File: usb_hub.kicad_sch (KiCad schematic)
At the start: 6 parts, among them U501 FE1.1s, Y501 12MHz

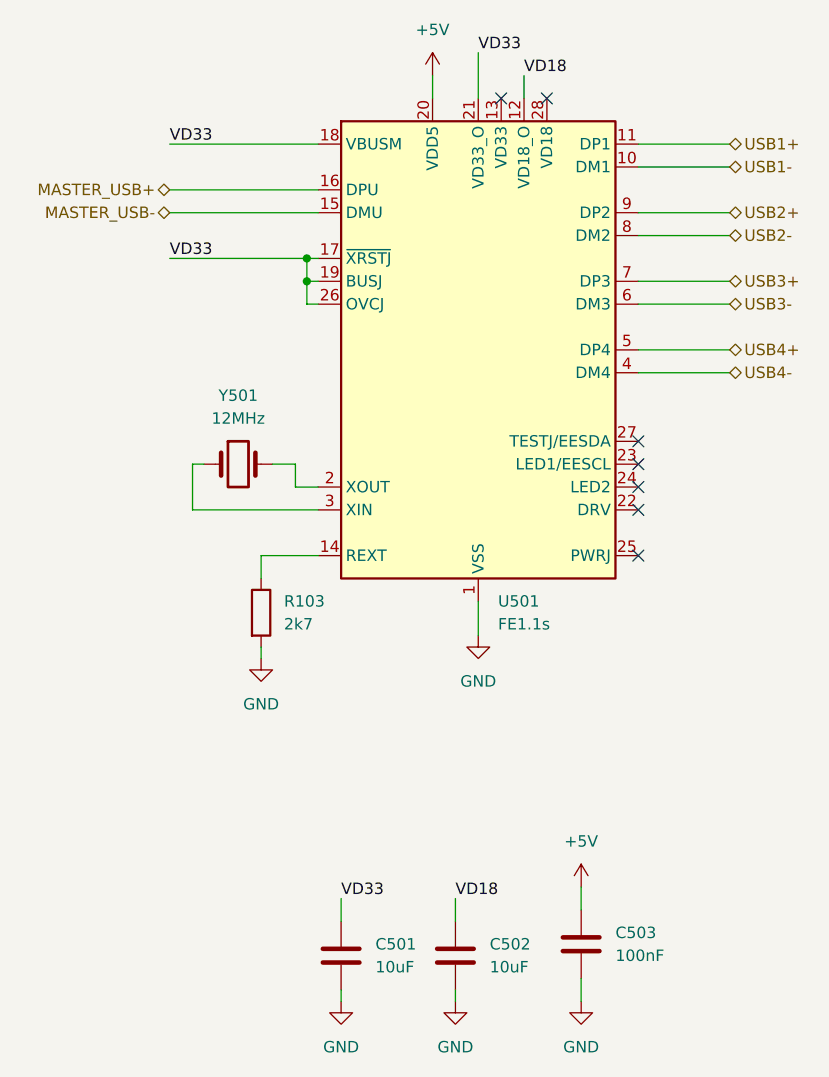
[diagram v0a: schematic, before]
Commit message: Update USB-C and USB-Hub Schematics with New Titles and Reference Changes
- Changed title from "DebugBoard" to "USB-C" in usb_c.kicad_sch.
- Changed title from "DebugBoard" to "USB-Hub" in usb_hub.kicad_sch.
- Updated multiple component references in usb_c.kicad_sch to new identifiers (#PWR0301 to #PWR0312, D301, U301, etc.).
- Updated component reference from "R103" to "R501" in usb_hub.kicad_sch.
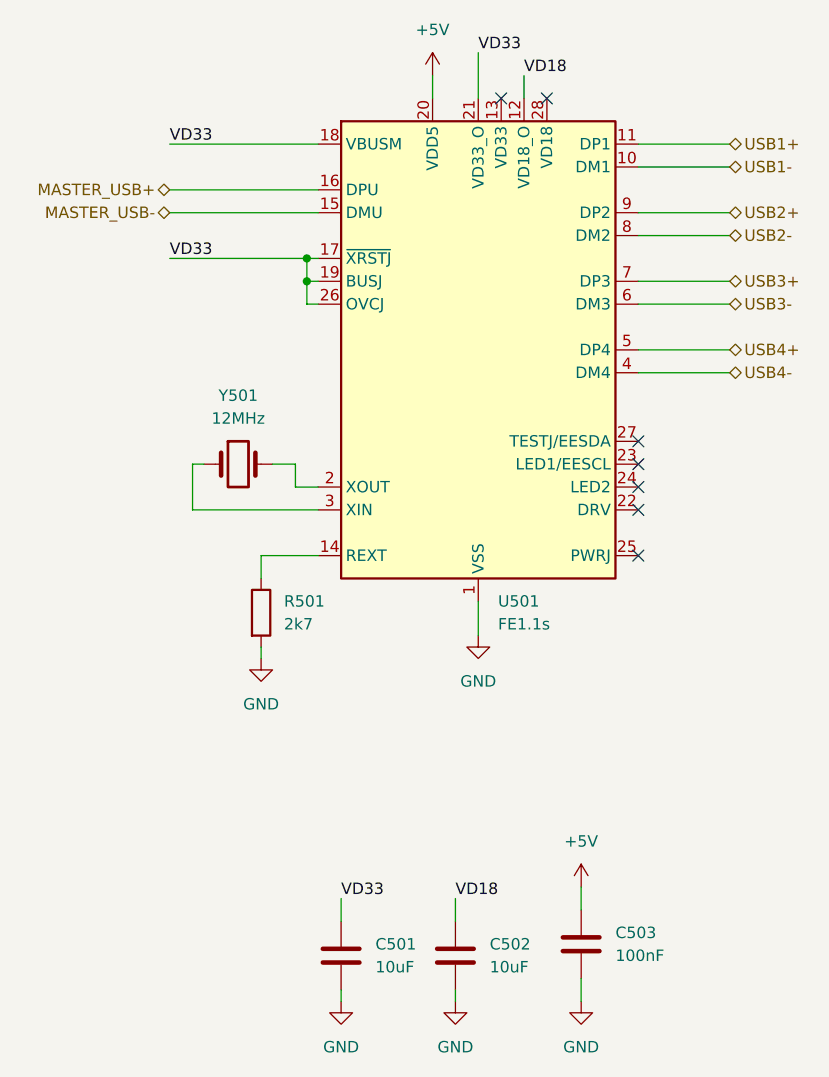
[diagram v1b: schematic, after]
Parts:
- renumbered R103 to R501
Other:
- title: DebugBoard -> USB-Hub
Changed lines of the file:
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@@
 	(paper "A4")
 	(title_block
-		(title "DebugBoard")
+		(title "USB-Hub")
 		(rev "<<HASH>>")
 		(company "Amateurfunkclub für Remote Stationen")
@@
 		(on_board yes)
 		(dnp no)
-		(property "Reference" "R103"
+		(property "Reference" "R501"
 			(at 110.49 104.1399 0)
 			(effects
@@
 			(project "main"
 				(path "/f228839c-6576-40b2-ae70-679b7b460639/77891167-0ccd-46b9-b393-55bbf8e2dec5"
-					(reference "R103")
+					(reference "R501")
 					(unit 1)
 				)
